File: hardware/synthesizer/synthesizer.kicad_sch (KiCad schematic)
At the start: 4 parts, among them J2 Input 2, J3 Input 1, J4 Output 1, J5 Output 2

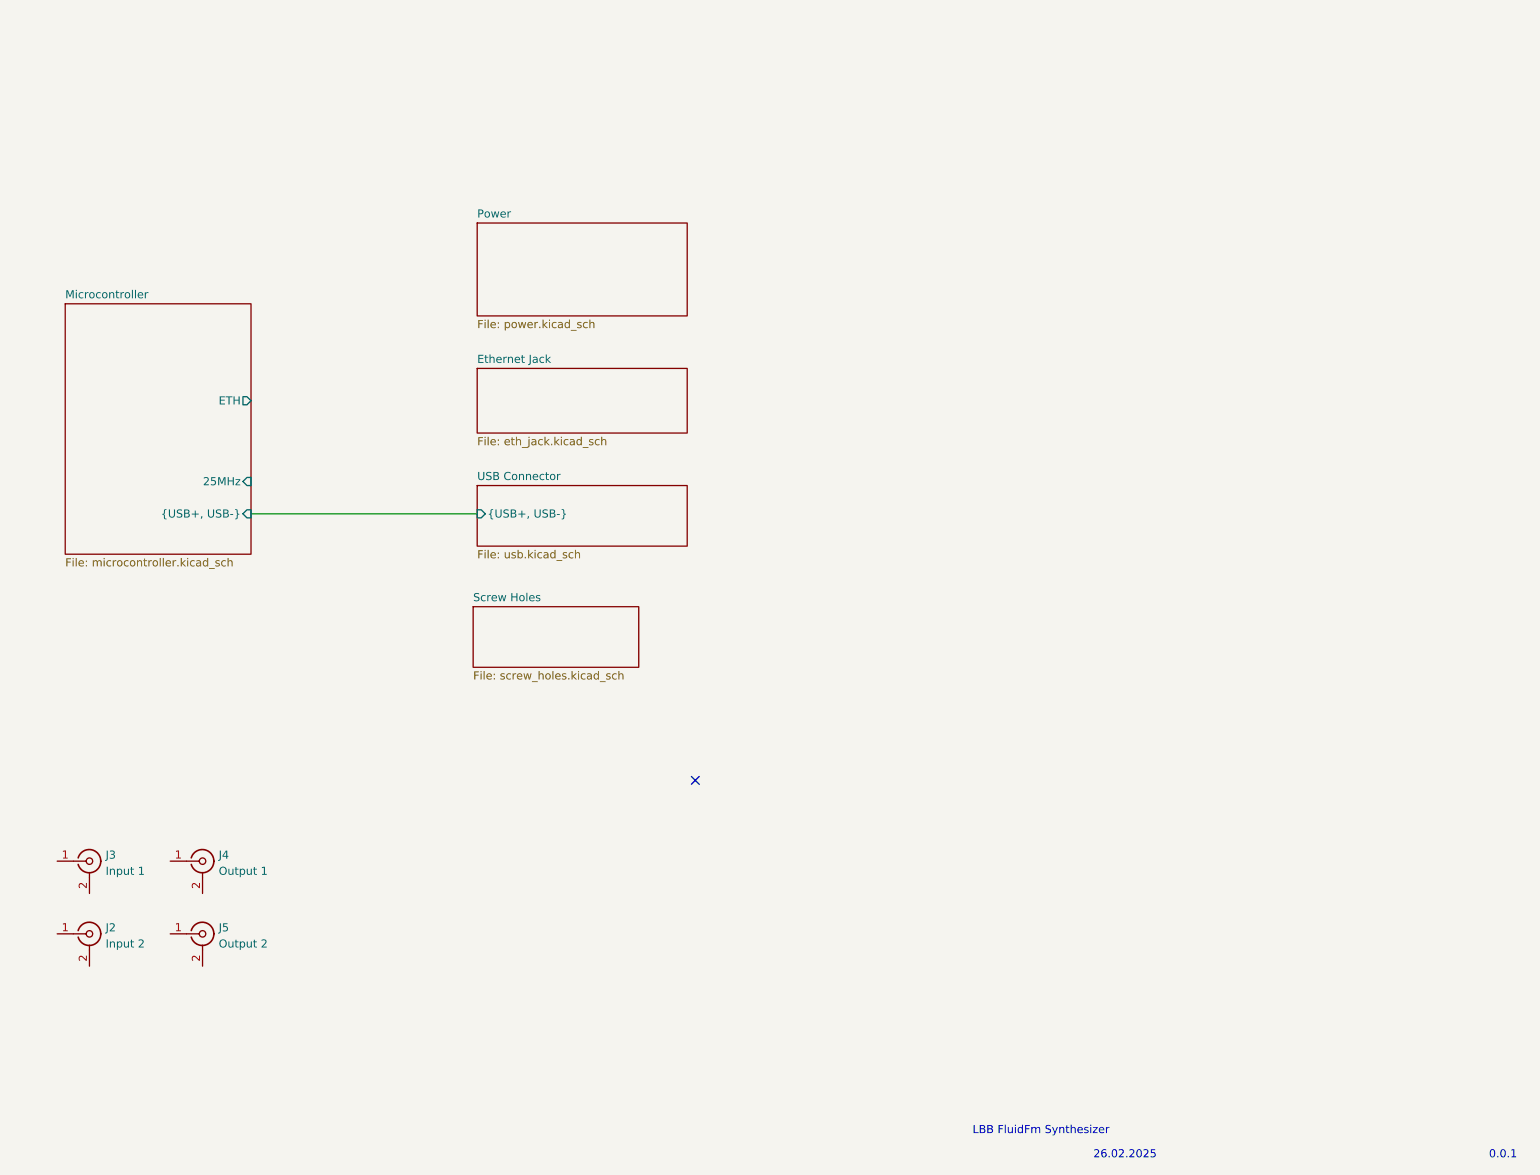
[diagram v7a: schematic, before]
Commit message: finish ethernet jack
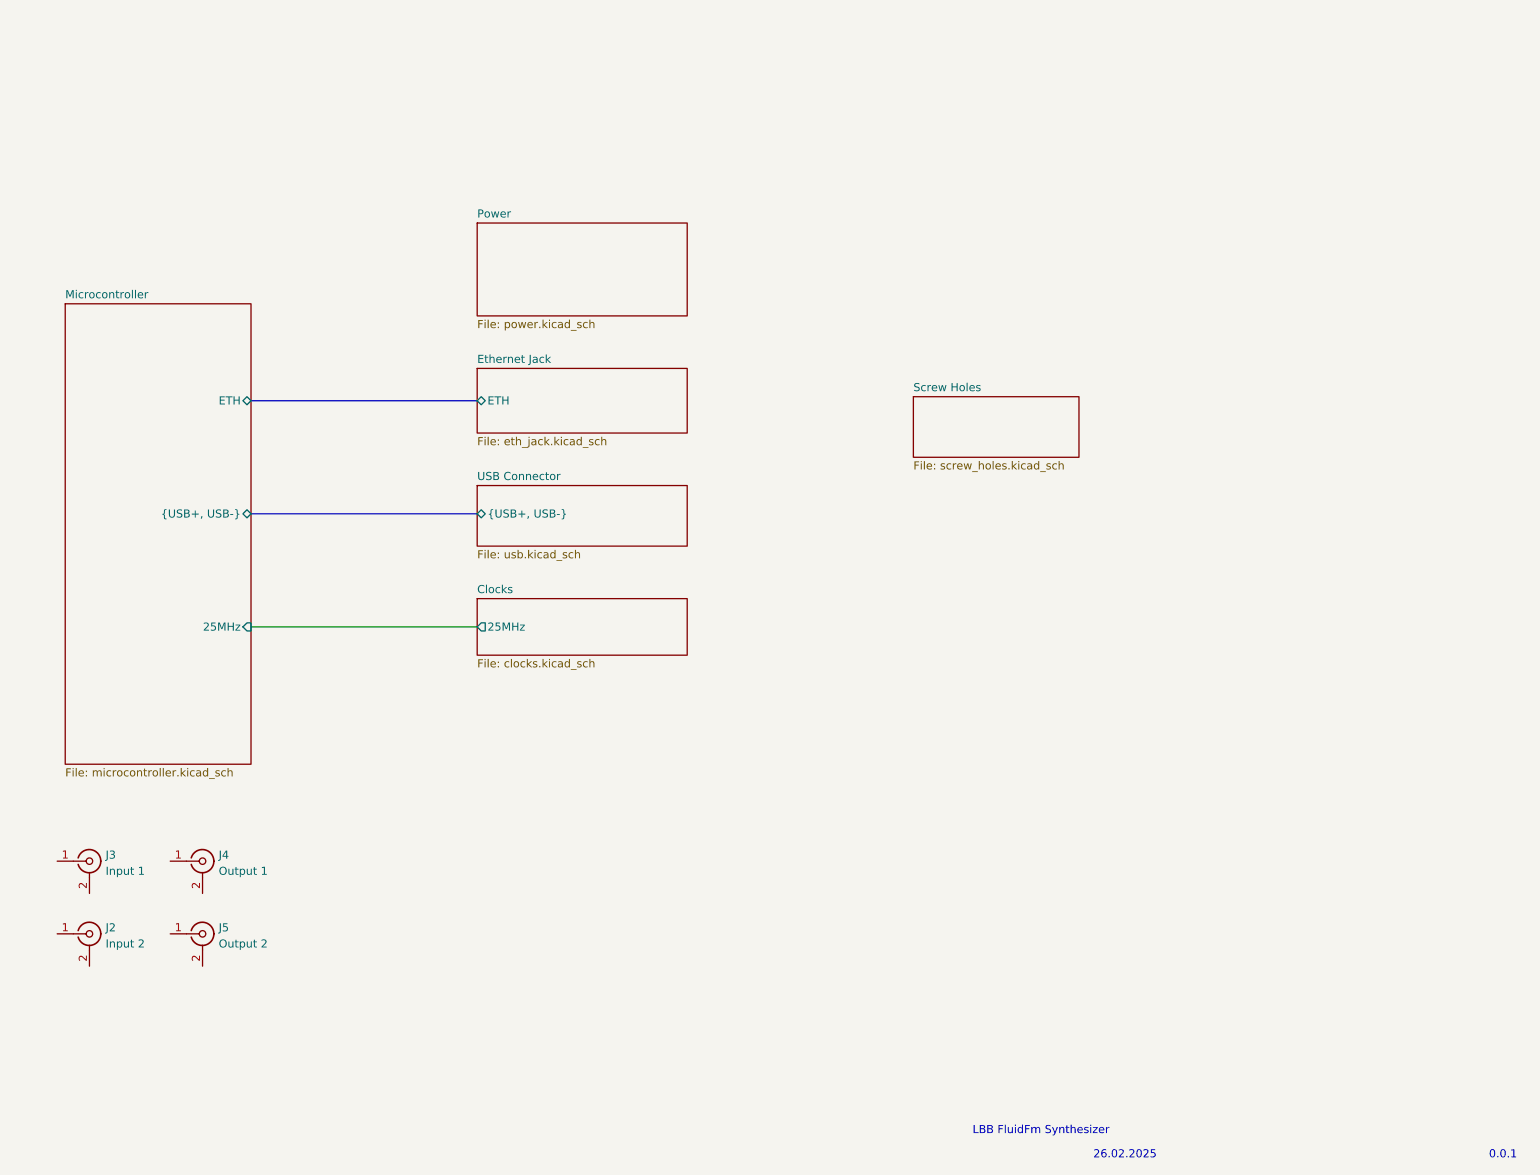
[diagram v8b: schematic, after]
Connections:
- no-connect marks 1 -> 0
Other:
- added sheet Clocks (clocks.kicad_sch)
- sheet Ethernet Jack ports: added ETH; removed none
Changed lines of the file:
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@@
 		)
-	)
-	(no_connect
-		(at 144.78 134.62)
 	)
 	(wire
 		(pts
+			(xy 74.93 110.49) (xy 110.49 110.49)
+		)
+		(stroke
+			(width 0)
+			(type default)
+		)
+	)
+	(bus
+		(pts
 			(xy 74.93 92.71) (xy 110.49 92.71)
+		)
+		(stroke
+			(width 0)
+			(type default)
+		)
+	)
+	(bus
+		(pts
+			(xy 74.93 74.93) (xy 110.49 74.93)
 		)
 		(stroke
@@
 			)
 		)
-		(pin "{USB+, USB-}" input
+		(pin "{USB+, USB-}" bidirectional
 			(at 110.49 92.71 180)
 			(effects
@@
 			)
 		)
+		(pin "ETH" bidirectional
+			(at 110.49 74.93 180)
+			(effects
+				(font
+					(size 1.27 1.27)
+				)
+				(justify left)
+			)
+		)
 		(instances
 			(project "synthesizer"
@@
 	)
 	(sheet
-		(at 109.855 107.315)
+		(at 179.07 74.295)
 		(size 26.035 9.525)
 		(exclude_from_sim no)
@@
 		)
 		(property "Sheetname" "Screw Holes"
-			(at 109.855 106.6034 0)
+			(at 179.07 73.5834 0)
 			(effects
 				(font
@@
 		)
 		(property "Sheetfile" "screw_holes.kicad_sch"
-			(at 109.855 117.4246 0)
+			(at 179.07 84.4046 0)
 			(effects
 				(font
@@
 	)
 	(sheet
-		(at 45.72 59.69)
-		(size 29.21 39.37)
+		(at 110.49 106.045)
+		(size 33.02 8.89)
 		(exclude_from_sim no)
 		(in_bom yes)
@@
 			(color 200 252 188 1.0000)
 		)
+		(property "Sheetname" "Clocks"
+			(at 110.49 105.3334 0)
+			(effects
+				(font
+					(size 1.27 1.27)
+				)
+				(justify left bottom)
+			)
+		)
+		(property "Sheetfile" "clocks.kicad_sch"
+			(at 110.49 115.5196 0)
+			(effects
+				(font
+					(size 1.27 1.27)
+				)
+				(justify left top)
+			)
+		)
+		(pin "25MHz" output
+			(at 110.49 110.49 180)
+			(effects
+				(font
+					(size 1.27 1.27)
+				)
+				(justify left)
+			)
+		)
+		(instances
+			(project "synthesizer"
+				(path "/f8740766-88d0-4c4d-b661-742f36f22c7b"
+					(page "7")
+				)
+			)
+		)
+	)
+	(sheet
+		(at 45.72 59.69)
+		(size 29.21 72.39)
+		(exclude_from_sim no)
+		(in_bom yes)
+		(on_board yes)
+		(dnp no)
+		(fields_autoplaced yes)
+		(stroke
+			(width 0.1524)
+			(type solid)
+		)
+		(fill
+			(color 200 252 188 1.0000)
+		)
 		(property "Sheetname" "Microcontroller"
 			(at 45.72 58.9784 0)
@@
 		)
 		(property "Sheetfile" "microcontroller.kicad_sch"
-			(at 45.72 99.6446 0)
+			(at 45.72 132.6646 0)
 			(effects
 				(font
@@
 			)
 		)
-		(pin "{USB+, USB-}" input
+		(pin "{USB+, USB-}" bidirectional
 			(at 74.93 92.71 0)
 			(effects
@@
 		)
 		(pin "25MHz" input
-			(at 74.93 87.63 0)
+			(at 74.93 110.49 0)
 			(effects
 				(font
@@
 			)
 		)
-		(pin "ETH" output
+		(pin "ETH" bidirectional
 			(at 74.93 74.93 0)
 			(effects
